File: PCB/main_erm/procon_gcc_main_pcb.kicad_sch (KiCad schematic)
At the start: 124 parts, among them J1 Conn_01x04_Pin, J3 To Button Board, J5 Conn_01x02_Pin, J9 USB_C_Receptacle, Q1 Q_PMOS_GDS, Q2 Q_NMOS_GSD, Q3 Q_NMOS_GSD, Q4 BSS138DW, Q5 BSS138DW, Q7 MMBT3904, Q8 MMBT3904, SW1 1TS026A-1000-0550, SW1 GL18_SW, SW2 GL18_SW, SW4 TS35CA, T1 36-8730, T2 36-8730, T3 36-8730, T4 36-8730, U1 GH39F (Hall SOT23), U10 MCP3002, U11 ST_LSM6, U12 PI3USB4000A, U16 BQ25180, U2 GD25Q80EEIGR, U2 GH39F (Hall SOT23), U3 GH39F (Hall SOT23), U4 GH39F (Hall SOT23), U4 TPS630001RCR, U5 ST_LSM6, U6 RP2040, U7 CH340K, U8 MCP3002, U9 ESP32-PICO-MINI-02, Y1 Crystal_GND3

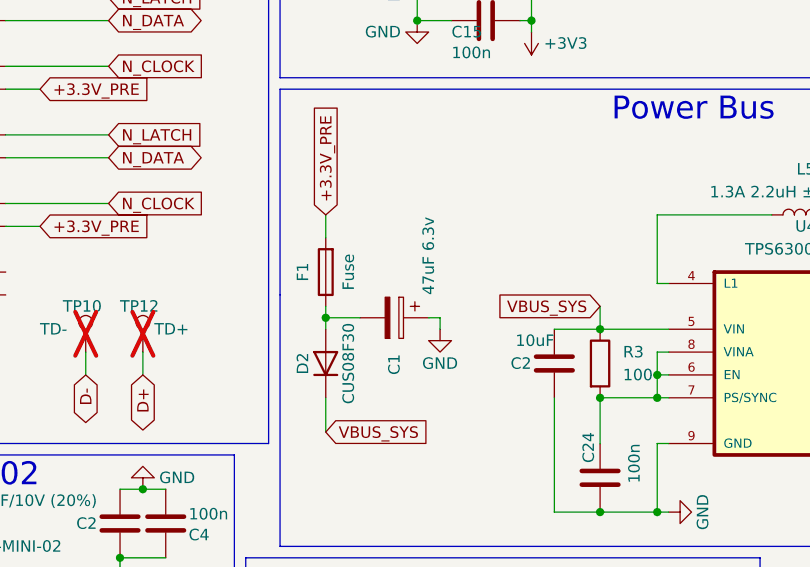
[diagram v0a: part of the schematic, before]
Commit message: PCB and FW Updates
- Add player number support internally
- Add debug for bt baseband updating
- Orange indication for baseband update mode
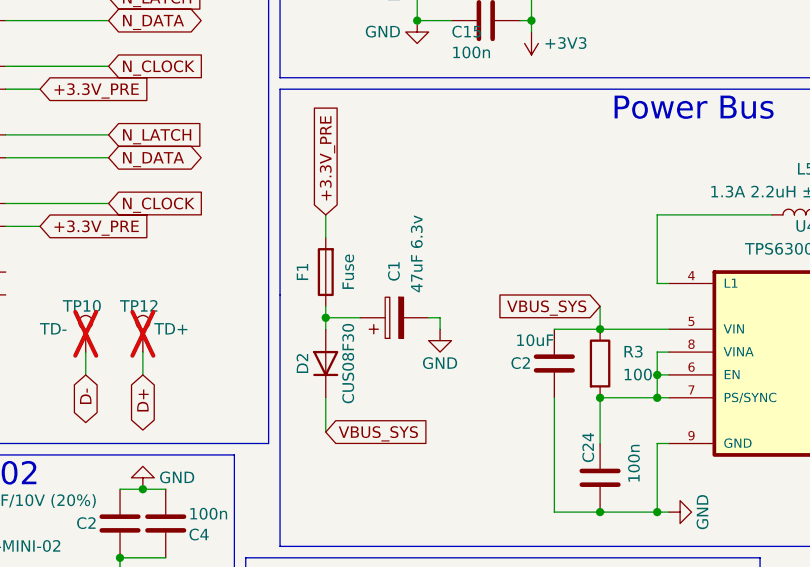
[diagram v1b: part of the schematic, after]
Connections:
- net GND: now also C1.2; no longer C1.1
- net at D2.2 (A), F1.1: now also C1.1; no longer C1.2
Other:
- moved on the sheet: C1
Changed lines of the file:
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@@
     )
   )
-  (symbol (lib_id "Device:C_Polarized") (at 86.36 176.53 270) (unit 1)
+  (symbol (lib_id "Device:C_Polarized") (at 86.36 176.53 90) (unit 1)
     (in_bom yes) (on_board yes) (dnp no)
-    (property "Reference" "C1" (at 86.36 182.88 0)
+    (property "Reference" "C1" (at 86.36 170.18 0)
       (effects (font (size 1.27 1.27)) (justify right))
     )
-    (property "Value" "47uF 6.3v" (at 90.17 173.99 0)
+    (property "Value" "47uF 6.3v" (at 88.9 165.1 0)
       (effects (font (size 1.27 1.27)) (justify right))
     )
-    (property "Footprint" "Capacitor_Tantalum_SMD:CP_EIA-3216-18_Kemet-A" (at 82.55 177.4952 0)
+    (property "Footprint" "Capacitor_Tantalum_SMD:CP_EIA-3216-18_Kemet-A" (at 90.17 175.5648 0)
       (effects (font (size 1.27 1.27)) hide)
     )
